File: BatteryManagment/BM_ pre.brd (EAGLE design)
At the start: 160 x 100 mm, 2 parts, among them U1 ATMEGA328P-AU

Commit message: Worked at the Schematic
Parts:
- added BATTERY+: Battery+, BM_pre:TESTPAD
- added BATTERY-: PAD, BM_pre:TESTPAD
- added C10, C11, C9: 10u, rcl:C0805
- added C2, C7: 100n, rcl:C0603
- added C3, C6: 47u, rcl:C1812
- added C4, C5: 100u, rcl:E3,5-10
- added C8: 1u_100V, rcl:C1206
- added CELL1, CELL2, CELL3, CELL4, CELL5, CELL6, GND, GND14, VIN: TPSQB2,54, testpad:B2,54
- added L1: 2310-V-RC, BM_pre:IND_23XX-V_53_53
- added R1: 100k, rcl:R0603
- added R10, R11, R12, R13, R2, R3, R4, R5, R6, R7, R8, R9: (no value), rcl:R0603
- added U$1, U$3, U$5: SBR10B45P5, BM_pre:POWERDI-5
- added U$2: IRFS7534-7PPBF, BM_pre:PG-TO263-7-3
- added U$4: CRA2512-FZ-R010ELF, BM_pre:R2512
- added U$6: IPB180P04P4L-02, BM_pre:PG-TO263-7-3
- added U$7: ZXTR2012Z, BM_pre:SOT89
- added U$8: NCV78L00A, BM_pre:SOIC8
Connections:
- removed net +3V3: C1.1, U1.18, U1.4, U1.6
- new net +12V: C10.1, U$7.3
- new net +5V: C1.1, C11.1, U$8.1, U1.18, U1.20, U1.4, U1.6
- new net ADC_BAT_1: R2.1, R3.2, U1.23
- new net ADC_BAT_2: R4.1, R5.2, U1.24
- new net ADC_BAT_3: R6.1, R7.2, U1.25
- new net ADC_BAT_4: R11.2, R8.1, U1.26
- new net ADC_BAT_5: R12.2, R9.1, U1.27
- new net ADC_BAT_6: R10.1, R13.2, U1.28
- new net BATTERY+: C9.1, R1.1, U$5.PAD, U$6.2, U$6.3, U$6.5, U$6.6, U$6.7, U$8.8
- new net CURRENT+: L1.2, U$4.1
- new net CURRENT-: C5.+, C6.1, C7.1, U$4.2, U$5.L, U$5.R
- new net CURRENTSENSE: U1.19
- new net LOAD_CONTROL: U$2.1
- new net MOTOR+: BATTERY+.P$1, U$6.8
- new net MOTOR_CONTROL: R1.2, U$6.1
- new net N$1: C2.1, C3.1, C4.+, U$1.PAD, U$2.2, U$2.3, U$2.5, U$2.6, U$2.7
- new net N$11: CELL3.TP, R6.2
- new net N$12: CELL4.TP, R8.2
- new net N$13: CELL5.TP, R9.2
- new net N$14: CELL6.TP, R10.2
- new net N$2: L1.1, U$2.8, U$3.PAD
- new net N$7: CELL1.TP, R2.2
- new net N$8: CELL2.TP, R4.2
- new net VIN_SENSE: C8.1, U$1.L, U$1.R, U$7.2, U$7.2@1, U1.22, VIN.TP
- net GND: now also BATTERY-.P$1, C10.2, C11.2, C2.2, C3.2, C4.-, C5.-, C6.2, C7.2, C8.2, C9.2, GND.TP, GND14.TP, R11.1, R12.1, R13.1, R3.1, R5.1, R7.1, U$3.L, U$3.R, U$7.1, U$8.2, U$8.3, U$8.6, U$8.7

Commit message: Upload it, that i can work at the PC
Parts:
- added R14, R15, R16, R17, R18, R19: (no value), rcl:R0603
- added U$10, U$11, U$12, U$13, U$14, U$15, U$16, U$17, U$18, U$19, U$20, U$9: BC817, BM_pre:SOT23
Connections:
- new net C1_B: U$15.1
- new net C2_B: U$16.1
- new net C3_B: U$17.1
- new net C4_B: U$18.1
- new net C5_B: U$19.1
- new net C6_B: U$20.1
- new net CELL1: CELL1.TP, R15.1, U$15.3, U$9.3
- new net CELL2: CELL2.TP, R16.1, U$10.3, U$16.3
- new net CELL3: CELL3.TP, R17.1, U$11.3, U$17.3
- new net CELL4: CELL4.TP, R18.1, U$12.3, U$18.3
- new net CELL5: CELL5.TP, R19.1, U$13.3, U$19.3
- new net CELL6: CELL6.TP, U$14.3, U$20.3
- new net N$10: R10.2, U$14.2
- new net N$3: R2.2, U$9.2
- new net N$4: R4.2, U$10.2
- new net N$5: R14.2, U$15.2
- new net N$6: R15.2, U$16.2
- new net N$9: R9.2, U$13.2
- new net V_MEAS: U$10.1, U$11.1, U$12.1, U$13.1, U$14.1, U$9.1
- net GND: now also R14.1
- net N$11: now also R16.2, U$17.2; no longer CELL3.TP, R6.2
- net N$12: now also R17.2, U$18.2; no longer CELL4.TP, R8.2
- net N$13: now also R18.2, U$19.2; no longer CELL5.TP, R9.2
- net N$14: now also R19.2, U$20.2; no longer CELL6.TP, R10.2
- net N$7: now also R6.2, U$11.2; no longer CELL1.TP, R2.2
- net N$8: now also R8.2, U$12.2; no longer CELL2.TP, R4.2

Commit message: schematic ready to layout
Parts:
- added C12: 100n, rcl:C0603
- added D1: 1N4004, diode:DO41-10
- added IC1: LMV321M5, BM_pre:SOT23-5
- added R20: 10k, rcl:R0603
- added R21, R22: 1k, rcl:R0603
- added R23, R24: 66k, rcl:R0603
- added SV1: (no value), con-lstb:MA03-2
- added U$21: BC817, BM_pre:SOT23
- added U2: LTC4440EMS8E-5PBF, BM_pre:MSOP-8_MS
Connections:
- removed net LOAD_CONTROL: U$2.1
- new net CHARGE_CONTROL: C12.2, D1.C, U$2.1, U2.7
- new net CHARGE_PWM: U1.7, U2.1
- new net MISO: SV1.6, U1.16
- new net MOSI: SV1.3, U1.15
- new net N$15: IC1.1, R21.1, R23.2
- new net N$16: IC1.3, R22.1, R24.2
- new net RESETICSP: R20.1, SV1.2, U1.29
- new net SCK: SV1.4, U1.17
- new net TS: L1.1, U$2.8, U$3.PAD, U2.8
- new net UC_M_CONT: U$21.1, U1.11
- net +12V: now also D1.A, U2.3
- net +5V: now also IC1.5, R20.2, SV1.5
- net C1_B: now also U1.30
- net C2_B: now also U1.31
- net C3_B: now also U1.32
- net C4_B: now also U1.1
- net C5_B: now also U1.2
- net C6_B: now also U1.9
- net CURRENT+: now also R21.2
- net CURRENT-: now also R22.2
- net CURRENTSENSE: now also IC1.4, R23.1, R24.1
- net GND: now also IC1.2, SV1.1, U$21.3, U2.2, U2.4
- net MOTOR_CONTROL: now also U$21.2
- net N$2: now also C12.1, U2.6; no longer L1.1, U$2.8, U$3.PAD
- net V_MEAS: now also U1.10

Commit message: just updating my pc
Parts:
- removed R2: (no value), rcl:R0603
- added LED1, LED2, LED3: (no value), eagle-ltspice:LED_1206
- added PAD1, PAD2: (no value), wirepad:SMD2,54-5,08
- added R25, R26, R27: 330, rcl:R0603
- added R28: (no value), rcl:R0603
- added R29, R30: 1M, rcl:R0603
- added U$22, U$23: IPB180P04P4L-02, BM_pre:PG-TO263-7-3
- added U$24: FDN306P, BM_pre:SOT23
- added U$25: FDN337N, BM_pre:SOT23
- C1: value (none) -> 100n
- GND, VIN: value TPSQB2,54 -> Battery+; device testpad:B2,54 -> BM_pre:TESTPAD
- moved U1 358.3 mm to (268.0, -185.4)
- moved U$2 134.7 mm to (64.8, 76.2)
- moved VIN 87.1 mm to (10.2, 71.1)
- moved GND 64.7 mm to (10.2, 39.4)
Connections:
- removed net N$3: R2.2, U$9.2
- new net N$17: LED2.C, U1.12
- new net N$18: LED1.C, U1.13
- new net N$19: LED3.C, U1.14
- new net N$20: PAD1.1, R29.1, U$24.1, U$25.3
- new net N$21: R29.2, U$24.2
- new net N$23: LED2.A, R27.1
- new net N$24: LED1.A, R26.1
- new net N$25: LED3.A, R25.1
- new net N$26: R28.1, U$21.3
- new net SELBSTERHALTUNG: R30.2, U$25.1, U1.8
- net +5V: now also R25.2, R26.2, R27.2
- net ADC_BAT_1: now also U$9.2; no longer R2.1
- net BATTERY+: now also U$22.2, U$22.3, U$22.5, U$22.6, U$22.7, U$23.2, U$23.3, U$23.5, U$23.6, U$23.7, U$24.3
- net GND: now also GND.P$1, PAD2.1, R28.2, R30.1, U$25.2, U2.5; no longer GND.TP, U$21.3
- net MOTOR+: now also U$22.8, U$23.8
- net MOTOR_CONTROL: now also U$22.1, U$23.1
- net VIN_SENSE: now also VIN.P$1; no longer VIN.TP

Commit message: layout update
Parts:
- added MOTOR+: Battery+, BM_pre:TESTPAD
- added MOTOR-: PAD, BM_pre:TESTPAD
- added R2, R31, R32, R33, R34, R35: (no value), rcl:R0603
- BATTERY-: value PAD -> Battery+
- CELL1, CELL2, CELL3, CELL4, CELL5, CELL6, GND14: value TPSQB2,54 -> (none); device testpad:B2,54 -> wirepad:SMD2,54-5,08
- moved U$23 738.1 mm to (97.5, 37.3), turned to 180 degrees
- moved U$22 720.6 mm to (109.0, 37.3), turned to 180 degrees
- moved U$25 716.5 mm to (-95.0, 12.2)
- moved R29 716.5 mm to (-86.1, 26.2)
- moved R30 716.5 mm to (-96.2, 5.84)
- moved U$24 716.5 mm to (-95.0, 19.8)
- moved PAD1 708.0 mm to (-7.65, 16.7)
- moved PAD2 707.6 mm to (-15.3, 16.7)
- moved R21 697.7 mm to (-28.0, 155.9)
- moved C12 697.7 mm to (-26.7, 129.3)
- moved D1 697.7 mm to (-16.5, 117.8)
- moved IC1 697.7 mm to (-26.7, 162.3)
- moved LED1 697.7 mm to (-26.7, 93.7)
- moved LED2 697.7 mm to (-26.7, 100.0)
- moved LED3 697.7 mm to (-26.7, 87.3)
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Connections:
- net BATTERY+: now also BATTERY+.P$1
- net CELL1: now also CELL1.1, R31.1; no longer CELL1.TP
- net CELL2: now also CELL2.1, R32.1; no longer CELL2.TP
- net CELL3: now also CELL3.1, R33.1; no longer CELL3.TP
- net CELL4: now also CELL4.1, R34.1; no longer CELL4.TP
- net CELL5: now also CELL5.1, R35.1; no longer CELL5.TP
- net CELL6: now also CELL6.1; no longer CELL6.TP
- net GND: now also GND14.1, MOTOR-.P$1, R2.1; no longer GND14.TP
- net MOTOR+: now also MOTOR+.P$1; no longer BATTERY+.P$1
- net N$11: now also R32.2
- net N$12: now also R33.2
- net N$13: now also R34.2
- net N$14: now also R35.2
- net N$5: now also R2.2
- net N$6: now also R31.2
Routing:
- net BATTERY+: track 0.00 -> 65.0 mm
- net MOTOR+: track 0.00 -> 38.3 mm
- net N$1: track 0.00 -> 34.2 mm
- net V_MEAS: track 0.00 -> 26.4 mm
- net GND: track 0.00 -> 26.1 mm
- net TS: track 0.00 -> 22.8 mm
- net CELL2: track 0.00 -> 14.7 mm
- net CELL5: track 0.00 -> 13.5 mm
- net CELL4: track 0.00 -> 13.4 mm
- net CELL3: track 0.00 -> 13.3 mm
- net CELL1: track 0.00 -> 13.2 mm
- net CELL6: track 0.00 -> 13.2 mm
- net VIN_SENSE: track 0.00 -> 9.10 mm
- net N$5: track 0.00 -> 4.63 mm
- net N$6: track 0.00 -> 4.58 mm
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- added copper zone on layer 1, net BATTERY+
- added copper zone on layer 1, net MOTOR+
- added copper zone on layer 1, net N$1
- added copper zone on layer 1, net VIN_SENSE
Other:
- board size 160 x 100 mm -> 120.9 x 100.1 mm

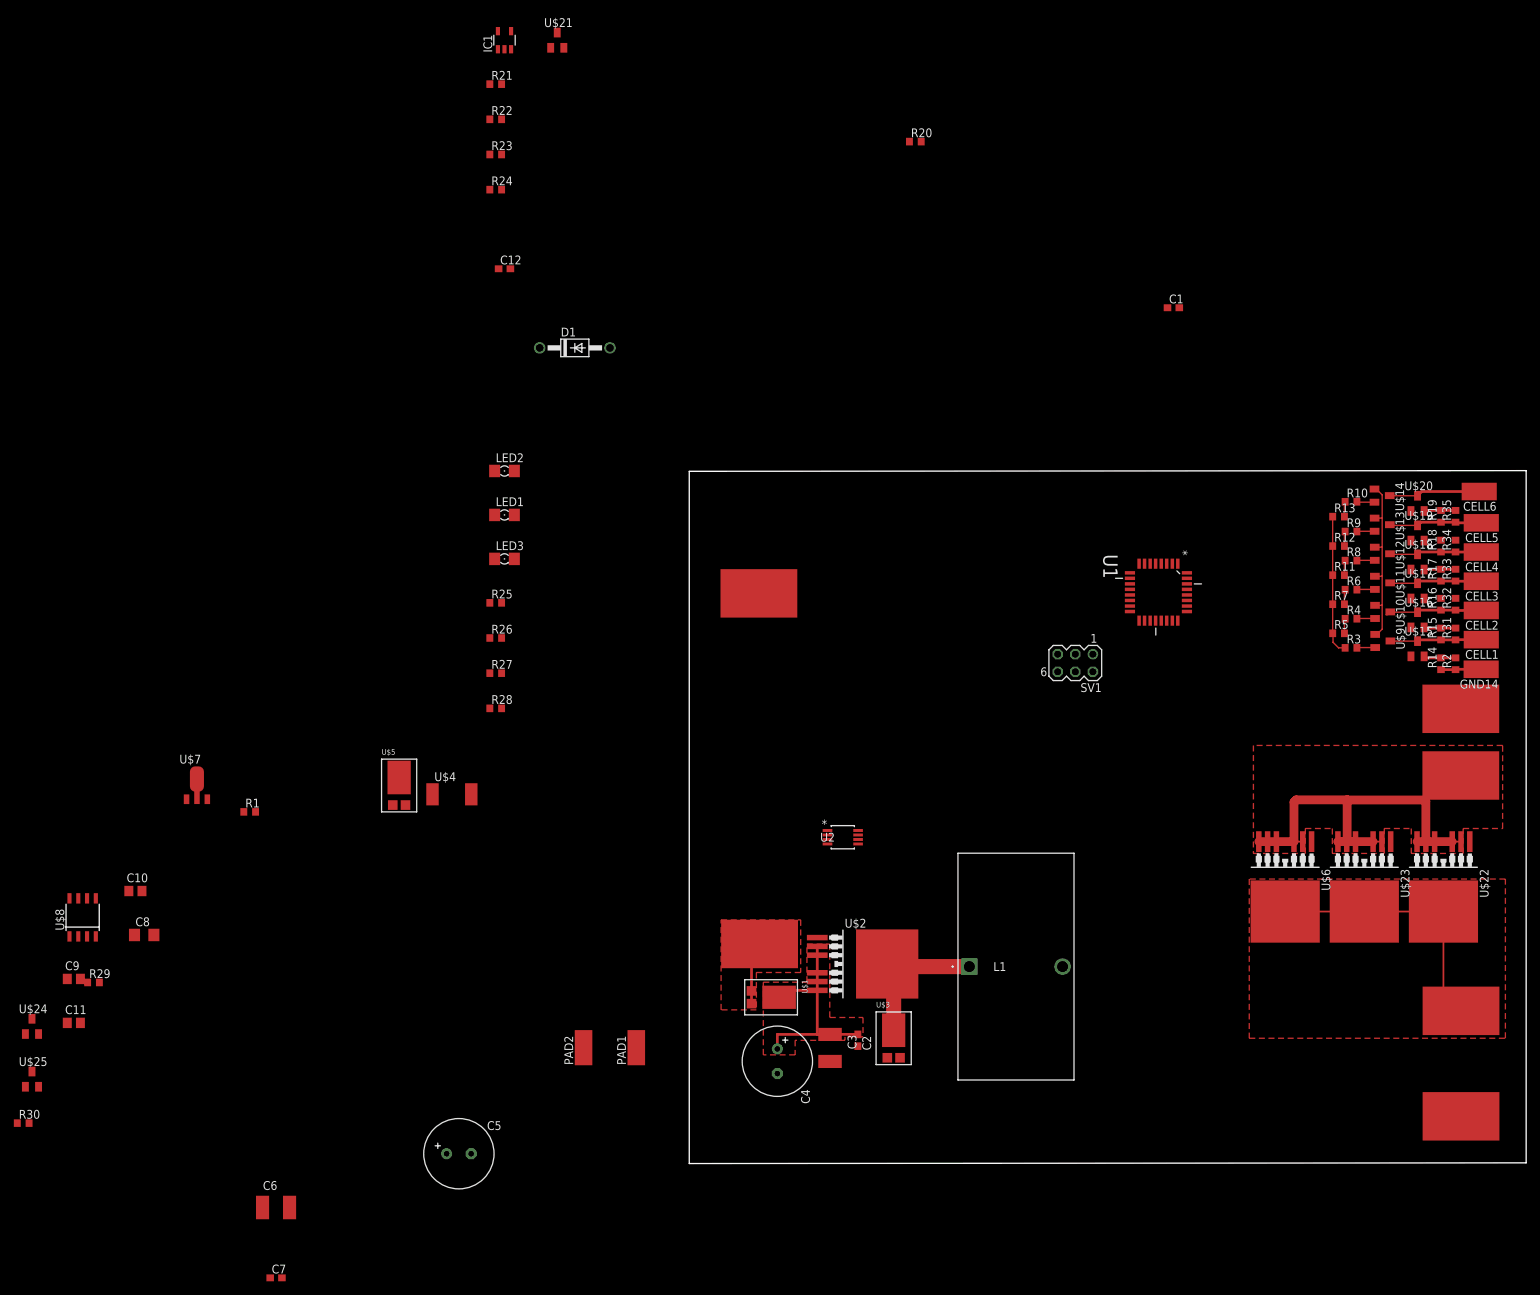
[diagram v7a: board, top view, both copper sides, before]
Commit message: Just GND Layout missing
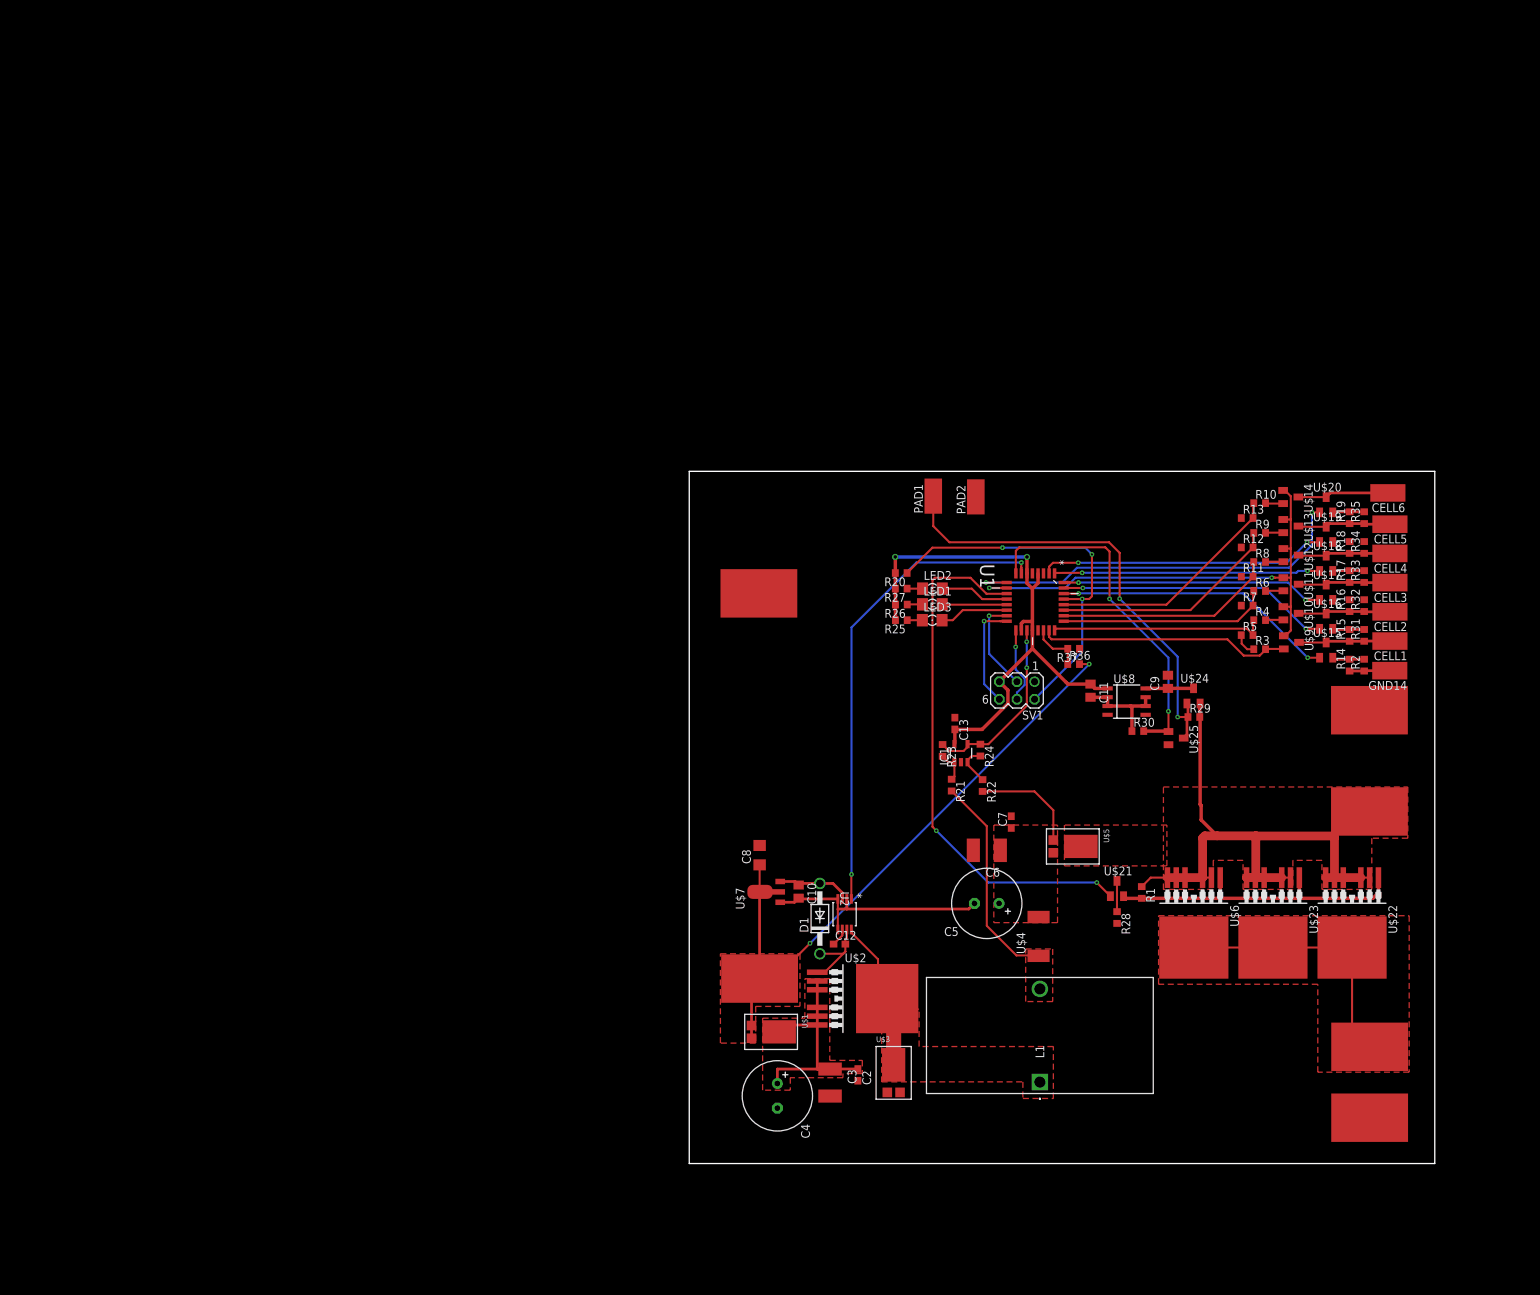
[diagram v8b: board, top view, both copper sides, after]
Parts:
- removed C1: 100n, eagle-ltspice:C0603
- added C13: 100n, eagle-ltspice:C0603
- added R36, R37: (no value), rcl:R0603
- moved U$24 174.5 mm to (72.8, 67.6)
- moved U$25 172.5 mm to (70.3, 61.5), turned to 270 degrees
- moved R30 170.7 mm to (64.8, 62.5)
- moved C9 163.8 mm to (69.2, 69.6), turned to 90 degrees
- moved R29 163.5 mm to (72.9, 64.5)
- moved C11 154.5 mm to (58.0, 68.3), turned to 270 degrees
- moved U$8 154.0 mm to (63.2, 66.7), turned to 270 degrees
- moved U$21 146.8 mm to (61.8, 39.7)
- moved R1 129.4 mm to (65.4, 39.2), turned to 270 degrees
- moved C7 125.0 mm to (46.5, 49.3), turned to 90 degrees
- moved IC1 122.3 mm to (39.3, 59.3)
- moved R21 120.8 mm to (37.9, 54.7), turned to 270 degrees
- moved R22 119.2 mm to (42.4, 54.6), turned to 270 degrees
- moved C6 114.9 mm to (43.0, 45.2), turned to 180 degrees
- moved C12 108.9 mm to (21.7, 31.7)
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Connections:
- removed net N$21: R29.2, U$24.2
- new net N$27: R36.1, R37.2, U1.22
- new net TEST: C9.1, U$24.3, U$8.8
- net +5V: now also C13.2; no longer C1.1
- net BATTERY+: now also R29.2, U$24.2; no longer C9.1, U$24.3, U$8.8
- net GND: now also C13.1, R37.1; no longer C1.2
- net VIN_SENSE: now also R36.2; no longer U1.22
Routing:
- net VIN_SENSE: track 9.10 -> 96.1 mm, vias 0 -> 2
- net +5V: track 0.00 -> 82.4 mm, vias 0 -> 2
- net UC_M_CONT: track 0.00 -> 77.3 mm, vias 0 -> 2
- net CHARGE_PWM: track 0.00 -> 69.2 mm, vias 0 -> 2
- net N$20: track 0.00 -> 66.9 mm, vias 0 -> 2
- net C6_B: track 0.00 -> 58.2 mm, vias 0 -> 2
- net RESETICSP: track 0.00 -> 56.3 mm, vias 0 -> 3
- net SELBSTERHALTUNG: track 0.00 -> 50.4 mm, vias 0 -> 2
- net V_MEAS: track 26.4 -> 72.1 mm, vias 0 -> 2
- net MOTOR_CONTROL: track 1.10 -> 46.6 mm
- net C5_B: track 0.00 -> 41.5 mm, vias 0 -> 2
- net C1_B: track 0.00 -> 40.8 mm, vias 0 -> 2
- net C2_B: track 0.00 -> 39.4 mm, vias 0 -> 2
- net C4_B: track 0.00 -> 38.4 mm, vias 0 -> 2
- net C3_B: track 0.00 -> 38.0 mm, vias 0 -> 2
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- added copper zone on layer 1, net CURRENT+
- added copper zone on layer 1, net CURRENT-
- added copper zone on layer 1, net TS
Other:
- board size 120.9 x 100.1 mm -> 107.7 x 100 mm
